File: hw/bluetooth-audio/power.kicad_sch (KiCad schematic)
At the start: 15 parts, among them J2 USB_C_Receptacle_USB2.0, U3 TLV71318PDBV, U5 USBLC6-2SC6, U7 NCP1117-3.3_SOT223

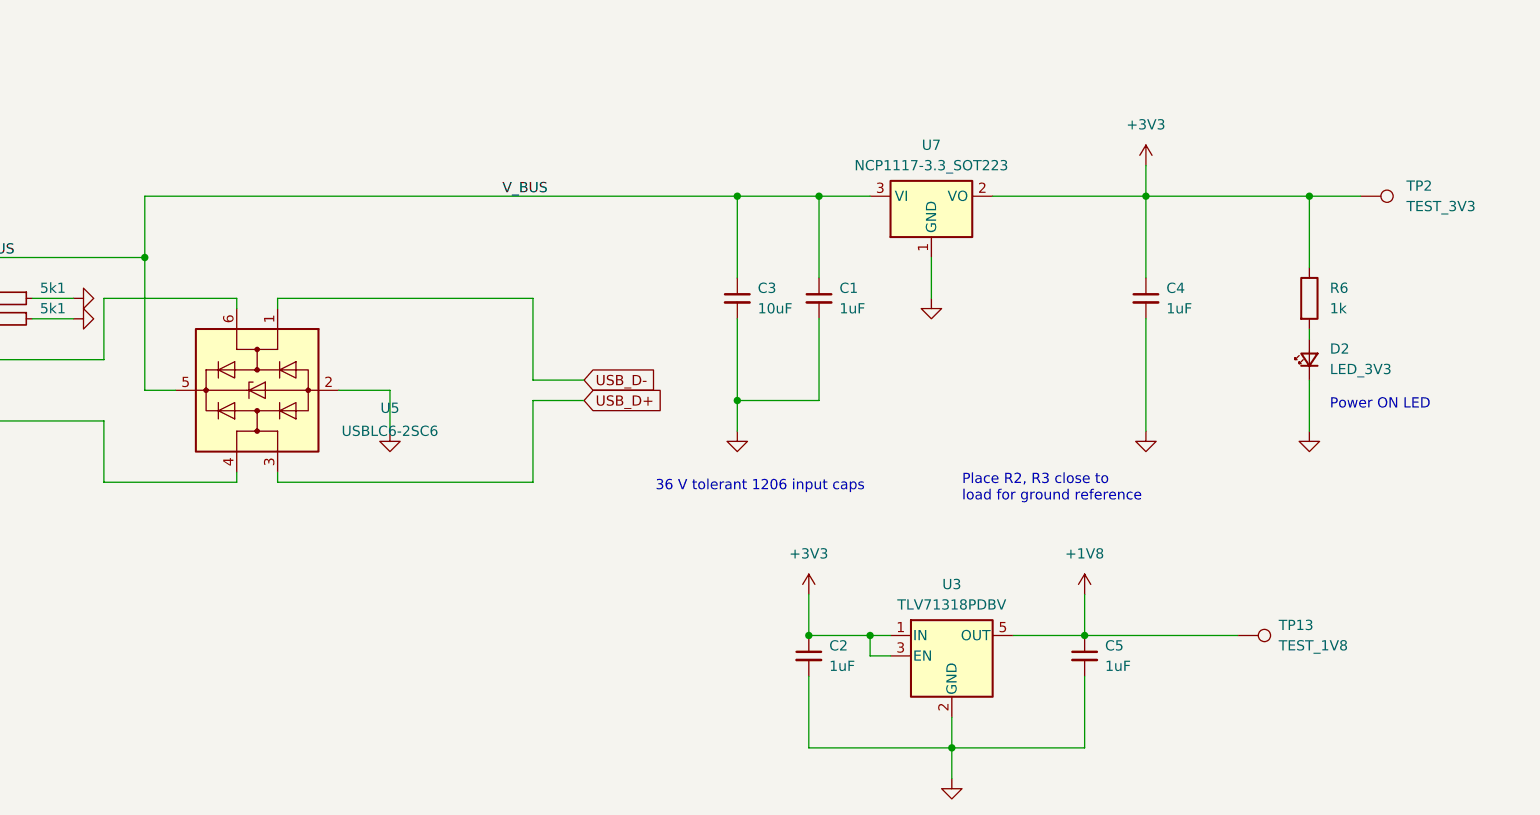
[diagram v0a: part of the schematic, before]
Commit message: Schematic: split supply into separate audio and system 3V3 rails
First design work since the April 2025 production release. Sixteen months of
edits had accumulated uncommitted; this captures the schematic and board state.

Power topology change: the single 3.3 V supply is now two independent rails,
+3V3_SYS and +3V3_AUDIO, each with its own regulator (U7, U8) and test point
(TEST_3V3_SYS, TEST_3V3_AUDIO). This isolates the ES8388 and the mic from the
~250 mA Bluetooth TX bursts on the ESP32 rail, which design-review-v1 flagged
as an S2 defect and the ES8388 user guide asks for directly.

Also addresses the S1 defects from the review (owner-applied): ES8388 CE pin
pulled down to DGND so the I2C address is determined rather than floating, and
the ESP32 CAP1 10 nF cap fitted.

Both rails are currently NCP1117-3.3 in SOT-223. The topology is right but the
parts are not yet the ones specified in docs/requirements-design.md: Rail A
should become AP7361C-33Y5 (SOT-89-5, ultra-low dropout, needed so the rail
survives on battery) and Rail B an LP5907MFX-3.3 (6.5 uVRMS, the point of
having a separate analog rail at all). Two SOT-223 parts also spend board area
the review specifically asked to reclaim.

Co-Authored-By: Claude Opus 5 <noreply@anthropic.com>
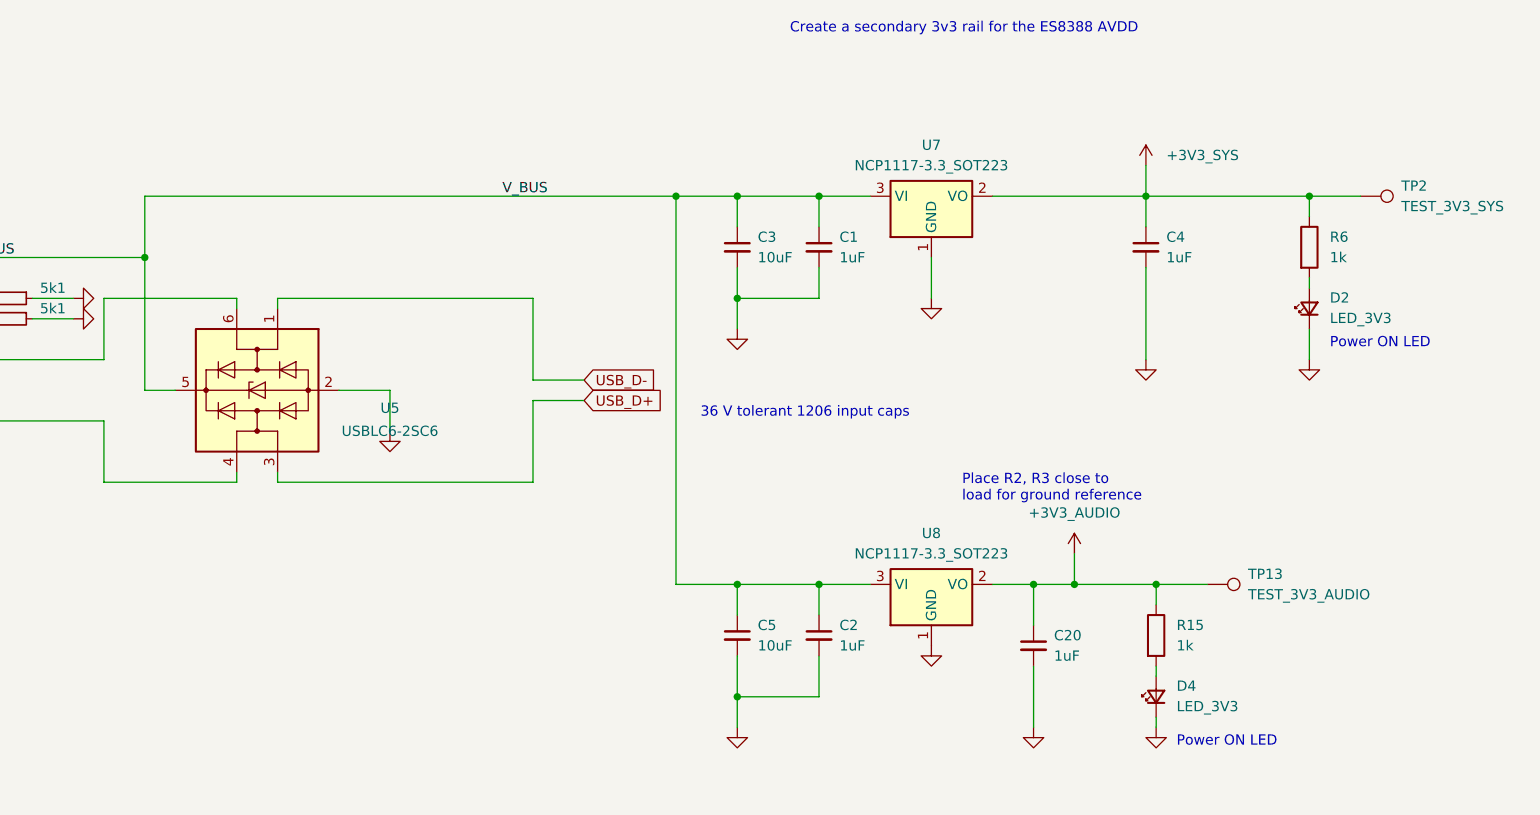
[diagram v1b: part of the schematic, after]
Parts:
- removed U3: TLV71318PDBV, Package_TO_SOT_SMD:SOT-23-5, symbol Regulator_Linear:TLV71318PDBV
- added C20: 1uF, Capacitor_SMD:C_0603_1608Metric, symbol Device:C_Small
- added D4: LED_3V3, LED_SMD:LED_0805_2012Metric, symbol Device:LED_Small
- added R15: 1k, Resistor_SMD:R_0402_1005Metric, symbol Device:R
- added U8: NCP1117-3.3_SOT223, Package_TO_SOT_SMD:SOT-223-3_TabPin2, symbol Regulator_Linear:NCP1117-3.3_SOT223
- C2: footprint Capacitor_SMD:C_0603_1608Metric -> Capacitor_SMD:C_1206_3216Metric
- C5: value 1uF -> 10uF; footprint Capacitor_SMD:C_0603_1608Metric -> Capacitor_SMD:C_1206_3216Metric
- TP13: value TEST_1V8 -> TEST_3V3_AUDIO
- TP2: value TEST_3V3 -> TEST_3V3_SYS
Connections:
- net GND: now also C20.2, D4.1 (K), U8.1 (GND)
- net USB_VBUS: now also C2.1, C5.1, U8.3 (VI)
- net +1V8 renamed +3V3_AUDIO
- net +3V3_AUDIO: now also C20.1, R15.1, U8.2 (VO); no longer C5.1
- net +3V3 renamed +3V3_SYS
- net +3V3_SYS: no longer C2.1
- new net: D4.2 (A), R15.2
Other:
- note added: "Create a secondary 3v3 rail for the ES8388 AVDD"
- moved on the sheet: C1, C3, C4, D2, R6

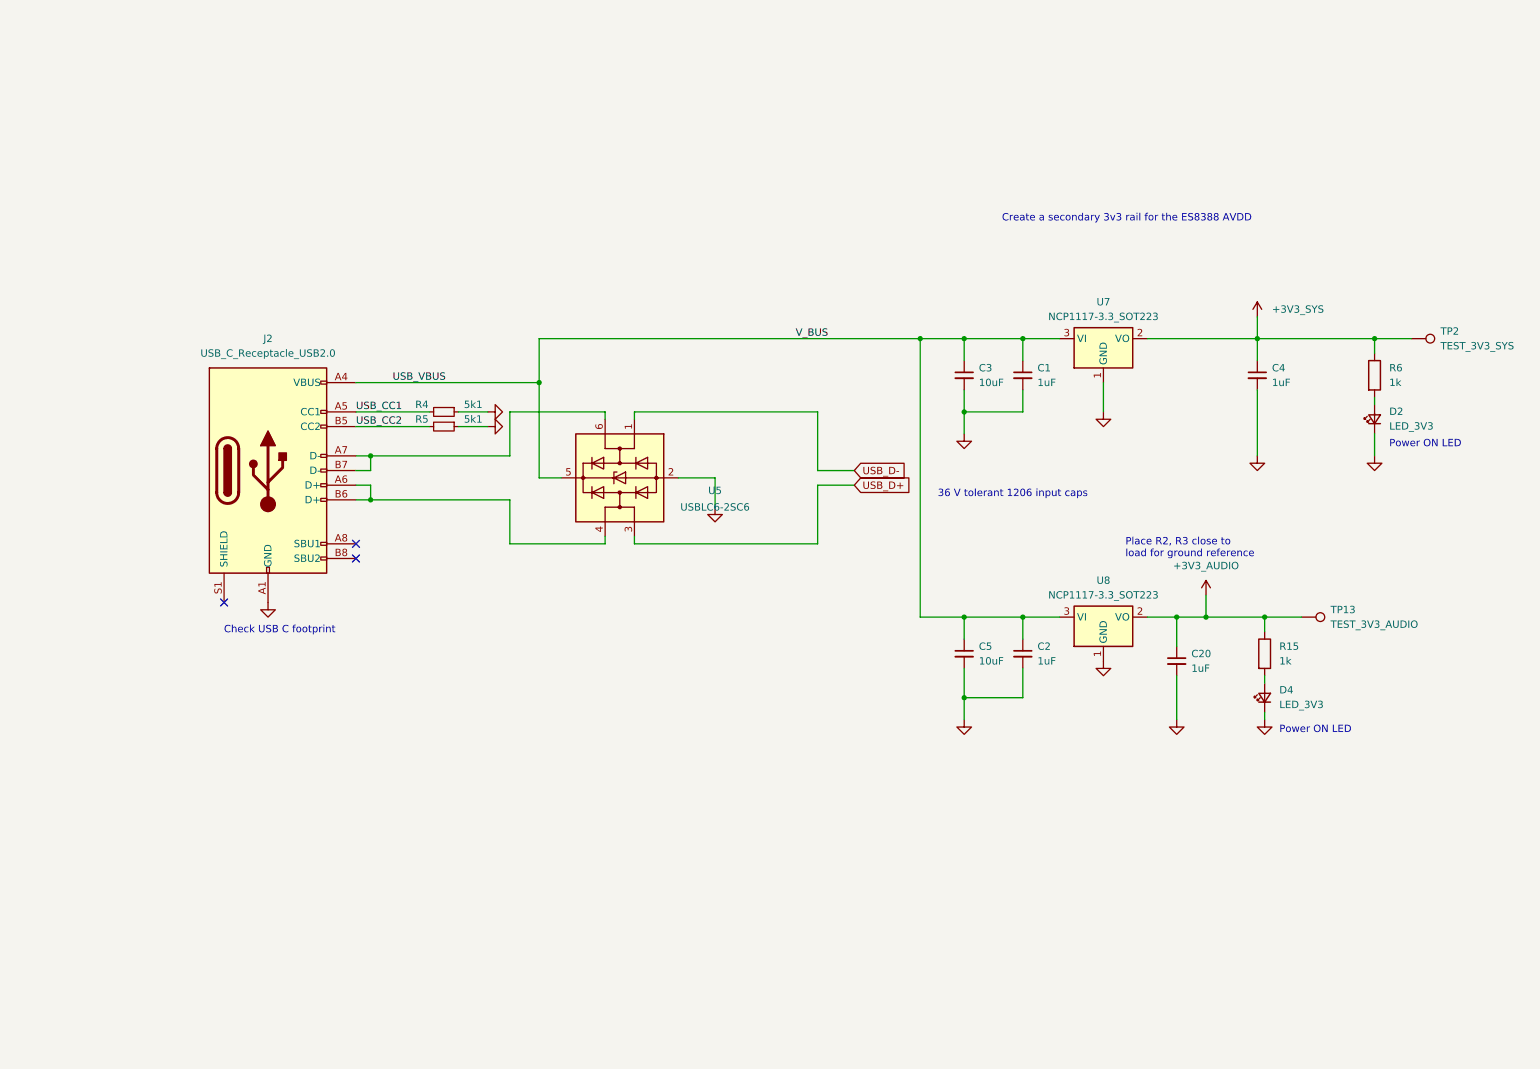
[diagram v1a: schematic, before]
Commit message: Power sheet: charger configuration, mode strapping and telemetry
Schematic (power sheet):
- R_ISET 4k7 -> 1k2 (742 mA fast charge), R_ILIM 3k -> 1k5 (1.073 A)
- EN1/EN2 strapping inverted and made overridable: R30 100k pulls EN1
  up to SYS, R31 100k pulls EN2 down. Default is now USB500, not the
  fixed ILIM strap -- 100 mA of USB100 cannot boot a 171 mA system on a
  flat cell, and USB500 is the mode that has VIN-DPM behind it.
- EN1, EN2, /PGOOD, /CHG, BAT_ADC, USB_CC1, USB_CC2 promoted to global
  labels, ready for the micro sheet.
- Status LED pull-ups R28/R29 moved SYS -> 3V3_A so /PGOOD and /CHG are
  3.3 V logic a GPIO can read; 4.4 V exceeds the ESP32 input rating.
- Add R34/R35 100k/100k battery divider (BAT_ADC) for state of charge.
- Add R36/R37 1k series taps on CC1/CC2 for source-capability sensing.

docs/design-overview.md:
- Section 3 expanded from a summary into the full power subsystem: the
  five power-path loops and their priority, EN1/EN2 mode strapping and
  why the default matters, charge programming with formulas and values,
  source capability detection and the A-to-C 56k limitation, safety
  timers, TS temperature qualification thresholds, status decoding,
  state-of-charge method and limits, and the power GPIO map.
- Section 2 power tree redrawn with control and telemetry signals.
- Section 7: charge current/time table and charger thermal analysis.
- Section 9: seven firmware dependencies covering limit sequencing, CC
  reads, /CHG fault decoding, SoC blindness while charging, the codec
  rail defaulting off, and CH340K gating.
- Deltas 13-16; open items now name what is not yet on the schematic.

audio.kicad_sch is pin-UUID churn from KiCad only, no netlist change.

Co-Authored-By: Claude Opus 5 <noreply@anthropic.com>
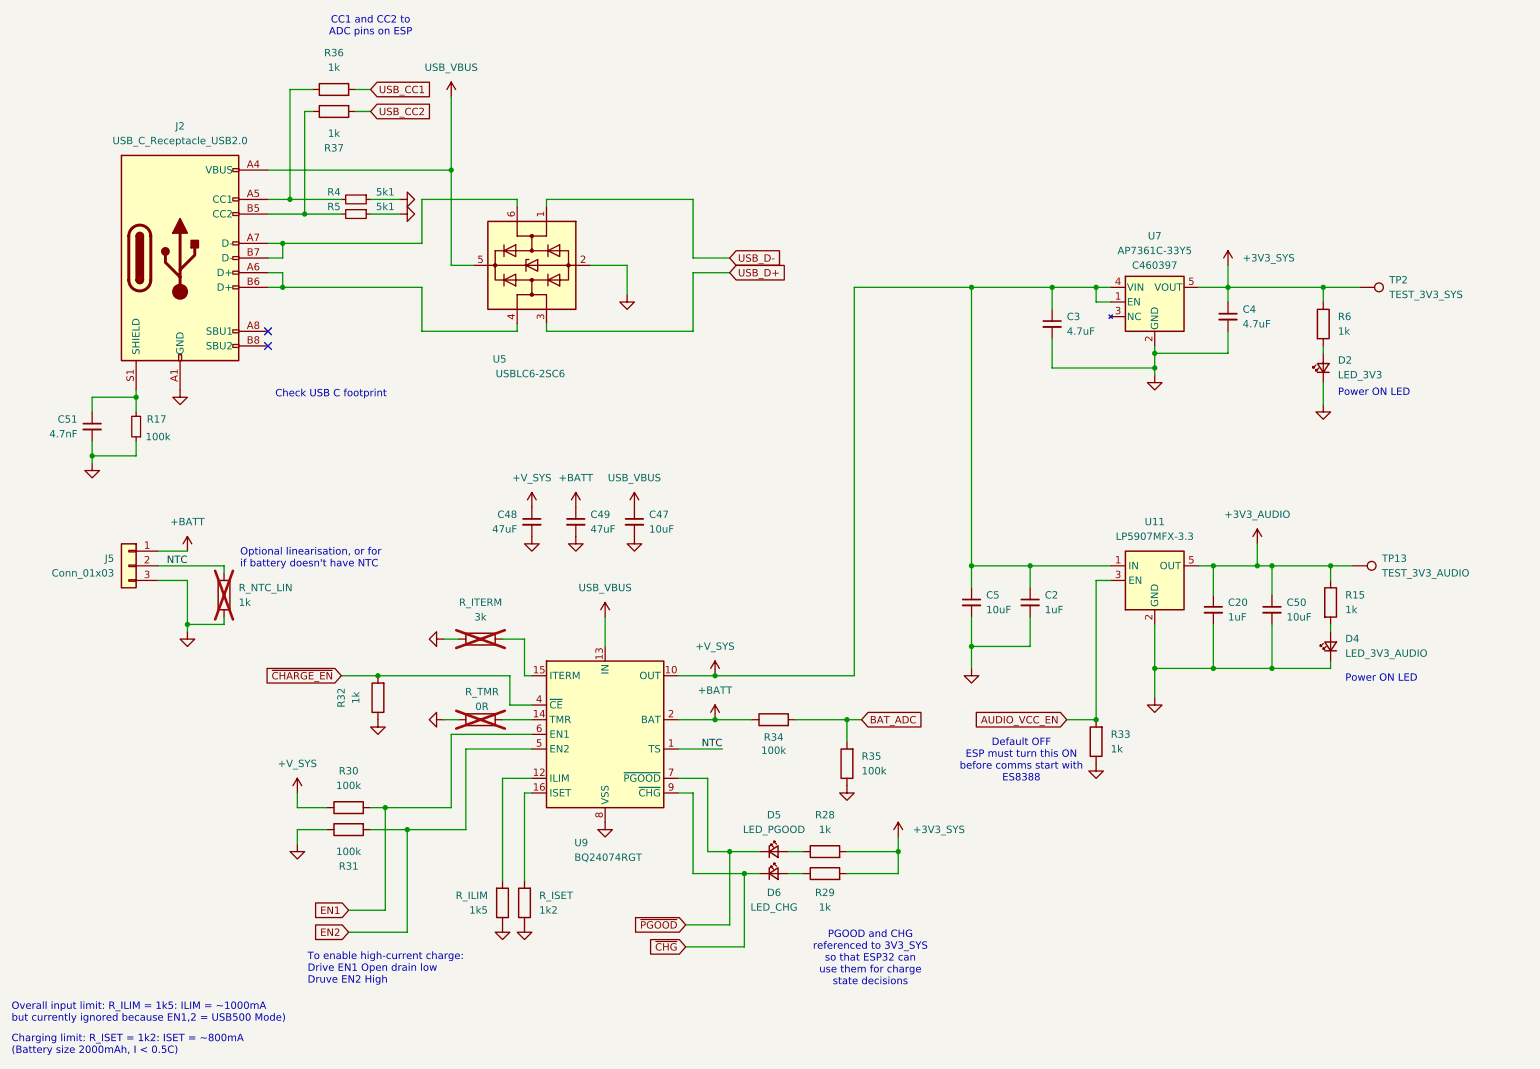
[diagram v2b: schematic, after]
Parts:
- removed C1: 1uF, Capacitor_SMD:C_1206_3216Metric, symbol Device:C_Small
- removed U7, U8: NCP1117-3.3_SOT223, Package_TO_SOT_SMD:SOT-223-3_TabPin2, symbol Regulator_Linear:NCP1117-3.3_SOT223
- added C47, C50: 10uF, Capacitor_SMD:C_1206_3216Metric, symbol Device:C_Small
- added C48, C49: 47uF, Capacitor_SMD:C_1206_3216Metric, symbol Device:C_Small
- added C51: 4.7nF, Capacitor_SMD:C_1206_3216Metric, symbol Device:C_Small
- added D5: LED_PGOOD, LED_SMD:LED_0805_2012Metric, symbol Device:LED_Small
- added D6: LED_CHG, LED_SMD:LED_0805_2012Metric, symbol Device:LED_Small
- added J5: Conn_01x03, Connector_Molex:Molex_Micro-Latch_53254-0370_1x03_P2.00mm_Horizontal, symbol Connector_Generic:Conn_01x03
- added R17: 100k, Resistor_SMD:R_0402_1005Metric, symbol Device:R_Small
- added R28, R29, R32, R33, R36, R37, R_NTC_LIN: 1k, Resistor_SMD:R_0402_1005Metric, symbol Device:R
- added R30, R31, R34, R35: 100k, Resistor_SMD:R_0402_1005Metric, symbol Device:R
- added R_ILIM: 1k5, Resistor_SMD:R_0402_1005Metric, symbol Device:R
- added R_ISET: 1k2, Resistor_SMD:R_0402_1005Metric, symbol Device:R
- added R_ITERM: 3k, Resistor_SMD:R_0402_1005Metric, symbol Device:R
- added R_TMR: 0R, Resistor_SMD:R_0402_1005Metric, symbol Device:R
- added U11: LP5907MFX-3.3, Package_TO_SOT_SMD:SOT-23-5, symbol Regulator_Linear:LP5907MFX-3.3
- added U7: AP7361C-33Y5, Package_TO_SOT_SMD:SOT-89-5, symbol custom_symbols:AP7361C-33Y5
- added U9: BQ24074RGT, Package_DFN_QFN:VQFN-16-1EP_3x3mm_P0.5mm_EP1.6x1.6mm, symbol Battery_Management:BQ24074RGT
- C3: value 10uF -> 4.7uF
- C4: value 1uF -> 4.7uF
- D4: value LED_3V3 -> LED_3V3_AUDIO
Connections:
- net +3V3_AUDIO: now also C50.1, U11.5 (OUT)
- net +3V3_SYS: now also R28.2, R29.2, U7.5 (VOUT)
- net GND: now also C47.2, C48.2, C49.2, C50.2, C51.2, J5.3 (Pin_3), R17.1, R31.1, R32.1, R33.1, R35.1, R_ILIM.1, R_ISET.1, R_ITERM.1, R_NTC_LIN.1, R_TMR.1, U11.2 (GND), U7.2 (GND), U9.17 (VSS), U9.8 (VSS)
- net USB_CC1: now also R36.2; no longer J2.A5 (CC1), R4.2
- net USB_CC2: now also R37.2; no longer J2.B5 (CC2), R5.2
- net USB_VBUS: now also C47.1, U9.13 (IN); no longer C2.1, C3.1, C5.1
- net at J2.S1 (SHIELD): now also C51.1, R17.2
- new net: J2.A5 (CC1), R36.1, R4.2
- new net: R_TMR.2, U9.14 (TMR)
- new net: J2.B5 (CC2), R37.1, R5.2
- new net: D6.2 (A), R29.1
- new net: R_ITERM.2, U9.15 (ITERM)
- new net: R_ILIM.2, U9.12 (ILIM)
- new net: R_ISET.2, U9.16 (ISET)
- new net: D5.2 (A), R28.1
- new net +BATT: C49.1, J5.1 (Pin_1), R34.1, U9.2 (BAT), U9.3 (BAT)
- new net +V_SYS: C2.1, C3.1, C48.1, C5.1, R30.1, U11.1 (IN), U7.1 (EN), U7.4 (VIN), U9.10 (OUT), U9.11 (OUT)
- new net AUDIO_VCC_EN: R33.2, U11.3 (EN)
- new net BAT_ADC: R34.2, R35.2
- new net EN1: R30.2, U9.6 (EN1)
- new net EN2: R31.2, U9.5 (EN2)
- new net NTC: J5.2 (Pin_2), R_NTC_LIN.2, U9.1 (TS)
- new net ~{CHARGE_EN}: R32.2, U9.4 (~{CE})
- new net ~{CHG}: D6.1 (K), U9.9 (~{CHG})
- new net ~{PGOOD}: D5.1 (K), U9.7 (~{PGOOD})
- no-connect marks 3 -> 2
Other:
- note added: "CC1 and CC2 to ADC pins on ESP"
- note added: "Charging limit: R_ISET = 1k2: ISET = ~800mA (Battery size 2000mAh, I < 0.5C)"
- note added: "Default OFF ESP must turn this ON before comms start with ES8388"
- note added: "Optional linearisation, or for if battery doesn't have NTC"
- note added: "Overall input limit: R_ILIM = 1k5: ILIM = ~1000mA but currently ignored because EN1,2 = USB500 Mode)"
- note added: "PGOOD and CHG referenced to 3V3_SYS so that ESP32 can use them for charge state decisions"
- note added: "To enable high-current charge: Drive EN1 Open drain low Druve EN2 High"
- note removed: "36 V tolerant 1206 input caps"
- note removed: "Create a secondary 3v3 rail for the ES8388 AVDD"
- note removed: "Place R2, R3 close to load for ground reference"
- moved on the sheet: C2, C20, C3, C4, C5, D2, D4, J2, R15, R4, R5, R6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

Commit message: Power sheet complete: ADC anti-droop caps, VBUS sense, LED brightness
Schematic (power sheet):
- R_ITERM 3k and R_TMR 56k populated (were DNP; R_TMR also still carried
  a 0R value, which grounds TMR and disables the safety timers rather
  than programming them).
- R28/R29 1k -> 330R. With the pull-ups now on 3V3_A instead of the
  4.4 V SYS rail, 1k gave ~0.9 mA and the LEDs were invisible again.
- C52 100nF on BAT_ADC, C53 100nF on USB_VBUS_SENSE. Both dividers sit
  well above Espressif's <10k source-impedance guideline (50k and 32k),
  so the SAR sample-and-hold would otherwise droop the node it is
  trying to measure.
- R38/R39 100k/47k VBUS sense divider. This is the guard rail for ILIM
  mode, which has no VIN-DPM and therefore no graceful foldback if
  source detection is ever wrong.

docs/design-overview.md:
- 3.4: guard-rail paragraph carries the real values, and explains why
  VBUS gets 100nF where BAT_ADC could take more.
- 3.4: CC ESD recorded as an accepted risk, with the reasoning, the
  bound on a VBUS-to-CC short, and the fix if it is ever wanted.
  Decided 2026-08-30, not mitigated in Rev B.
- 3.7: expanded the ADC capacitor rationale -- charge reservoir first,
  low-pass second, and why a lower-impedance divider was the worse
  trade. Notes the 330R LED value and its headroom against the 5 mA
  the status pins may sink.
- 10: open items trimmed to what actually remains; accepted risks
  called out separately.

Co-Authored-By: Claude Opus 5 <noreply@anthropic.com>
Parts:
- added C52, C53: 100nF, Capacitor_SMD:C_1206_3216Metric, symbol Device:C_Small
- added R38: 100k, Resistor_SMD:R_0402_1005Metric, symbol Device:R_Small
- added R39: 47k, Resistor_SMD:R_0402_1005Metric, symbol Device:R_Small
- R15, R28, R29, R6: value 1k -> 330R
- R_ITERM: now fitted
- R_TMR: value 0R -> 56k; now fitted
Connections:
- net BAT_ADC: now also C52.1
- net GND: now also C52.2, C53.2, R39.1
- net USB_VBUS: now also R38.2
- new net USB_VBUS_SENSE: C53.1, R38.1, R39.2
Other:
- note added: "SENSE measurement to ESP ADC"
- moved on the sheet: R34, R35
